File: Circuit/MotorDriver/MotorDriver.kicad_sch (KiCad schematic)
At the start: 28 parts, among them J3 Conn_01x03_Pin, J4 Conn_01x04_Pin, J5 Conn_01x06_Pin, J6 Conn_01x02_Pin, U3 DRV8316RRGFR, U4 XC6206P332MR-G

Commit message: フットプリントの割り当て完了
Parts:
- J3: footprint (none) -> OU_conn:MotorABC
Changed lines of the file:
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@@
 			)
 		)
-		(property "Footprint" ""
+		(property "Footprint" "OU_conn:MotorABC"
 			(at 132.08 140.97 0)
 			(hide yes)

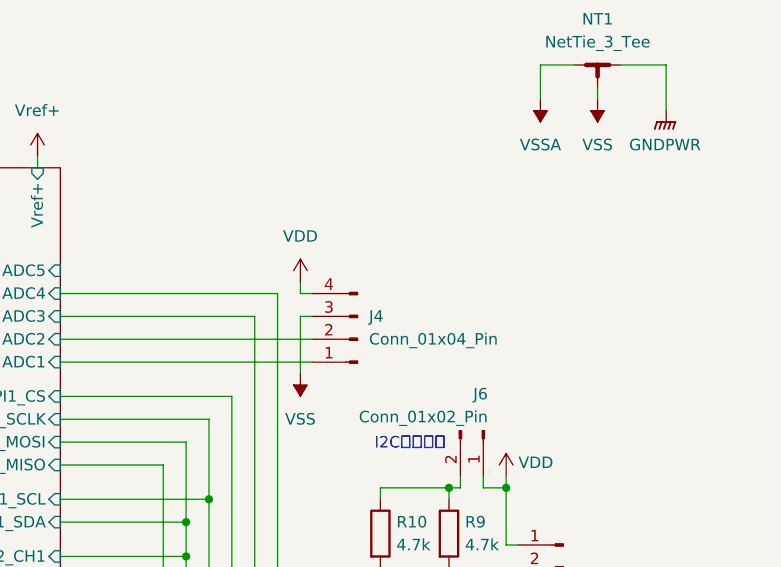
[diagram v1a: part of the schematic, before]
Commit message: フットプリントとシンボルを修正
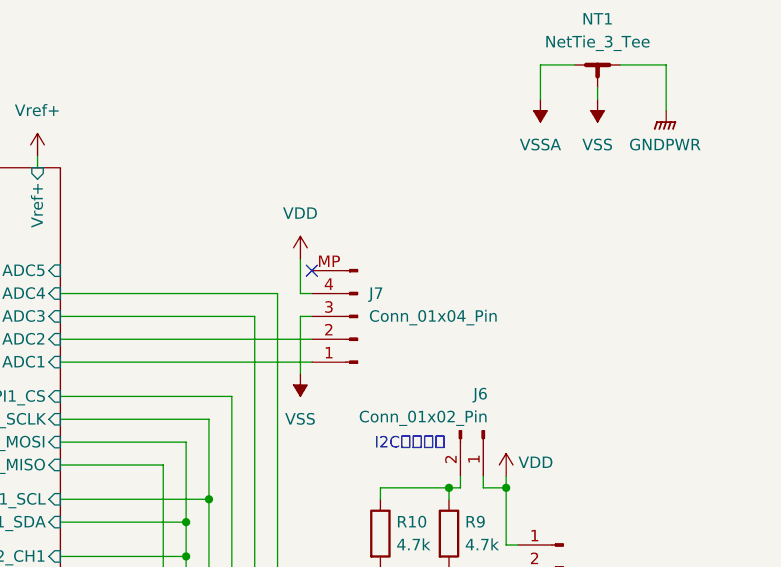
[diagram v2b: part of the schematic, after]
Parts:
- removed J4: Conn_01x04_Pin, Connector_JST:JST_GH_SM04B-GHS-TB_1x04-1MP_P1.25mm_Horizontal, symbol Connector:Conn_01x04_Pin
- added J7: Conn_01x04_Pin, Connector_JST:JST_GH_SM04B-GHS-TB_1x04-1MP_P1.25mm_Horizontal, symbol Connector:Conn_01x05_Pin
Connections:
- net STM32G4/ADC1: now also J7.1 (Pin_1)
- net STM32G4/ADC2: now also J7.2 (Pin_2)
- net VDD: now also J7.4 (Pin_4)
- net VSS: now also J7.3 (Pin_3)
- no-connect marks 3 -> 4
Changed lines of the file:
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@@
 	)
 	(no_connect
+		(at 146.05 59.69)
+	)
+	(no_connect
 		(at 123.19 172.72)
 	)
@@
 	(wire
 		(pts
-			(xy 144.78 60.96) (xy 144.78 62.23)
+			(xy 144.78 58.42) (xy 144.78 62.23)
 		)
 		(stroke
@@
 	)
 	(symbol
-		(lib_id "Connector:Conn_01x04_Pin")
-		(at 151.13 67.31 180)
-		(unit 1)
-		(body_style 1)
-		(exclude_from_sim no)
-		(in_bom yes)
-		(on_board yes)
-		(in_pos_files yes)
-		(dnp no)
-		(property "Reference" "J4"
-			(at 152.4 64.7699 0)
-			(show_name no)
-			(do_not_autoplace no)
-			(effects
-				(font
-					(size 1.27 1.27)
-				)
-				(justify right)
-			)
-		)
-		(property "Value" "Conn_01x04_Pin"
-			(at 152.4 67.3099 0)
-			(show_name no)
-			(do_not_autoplace no)
-			(effects
-				(font
-					(size 1.27 1.27)
-				)
-				(justify right)
-			)
-		)
-		(property "Footprint" "Connector_JST:JST_GH_SM04B-GHS-TB_1x04-1MP_P1.25mm_Horizontal"
-			(at 151.13 67.31 0)
-			(hide yes)
-			(show_name no)
-			(do_not_autoplace no)
-			(effects
-				(font
-					(size 1.27 1.27)
-				)
-			)
-		)
-		(property "Datasheet" ""
-			(at 151.13 67.31 0)
-			(hide yes)
-			(show_name no)
-			(do_not_autoplace no)
-			(effects
-				(font
-					(size 1.27 1.27)
-				)
-			)
-		)
-		(property "Description" "Generic connector, single row, 01x04, script generated"
-			(at 151.13 67.31 0)
-			(hide yes)
-			(show_name no)
-			(do_not_autoplace no)
-			(effects
-				(font
-					(size 1.27 1.27)
-				)
-			)
-		)
-		(pin "1"
-		)
-		(pin "2"
-		)
-		(pin "4"
-		)
-		(pin "3"
-		)
-		(instances
-			(project "MotorDriver"
-				(path "/0d88f791-841b-4934-8770-7a8a0368e67c"
-					(reference "J4")
-					(unit 1)
-				)
-			)
-		)
-	)
-	(symbol
 		(lib_id "power:VSS")
 		(at 172.6592 198.12 180)
@@
 	(symbol
 		(lib_id "power:VDD")
-		(at 144.78 60.96 0)
+		(at 144.78 58.42 0)
 		(unit 1)
 		(body_style 1)
@@
 		(fields_autoplaced yes)
 		(property "Reference" "#PWR043"
-			(at 144.78 64.77 0)
+			(at 144.78 62.23 0)
 			(hide yes)
 			(show_name no)
@@
 		)
 		(property "Value" "VDD"
-			(at 144.78 55.88 0)
+			(at 144.78 53.34 0)
 			(show_name no)
 			(do_not_autoplace no)
@@
 		)
 		(property "Footprint" ""
-			(at 144.78 60.96 0)
+			(at 144.78 58.42 0)
 			(hide yes)
 			(show_name no)
@@
 		)
 		(property "Datasheet" ""
-			(at 144.78 60.96 0)
+			(at 144.78 58.42 0)
 			(hide yes)
 			(show_name no)
@@
 		)
 		(property "Description" "Power symbol creates a global label with name \"VDD\""
-			(at 144.78 60.96 0)
+			(at 144.78 58.42 0)
 			(hide yes)
 			(show_name no)
@@
 					(unit 1)
 				)
+			)
+		)
+	)
+	(symbol
+		(lib_id "Connector:Conn_01x05_Pin")
+		(at 151.13 64.77 180)
+		(unit 1)
+		(body_style 1)
+		(exclude_from_sim no)
+		(in_bom yes)
+		(on_board yes)
+		(in_pos_files yes)
+		(dnp no)
+		(property "Reference" "J7"
+			(at 152.4 62.2299 0)
+			(show_name no)
+			(do_not_autoplace no)
+			(effects
+				(font
+					(size 1.27 1.27)
+				)
+				(justify right)
+			)
+		)
+		(property "Value" "Conn_01x04_Pin"
+			(at 152.4 64.7699 0)
+			(show_name no)
+			(do_not_autoplace no)
+			(effects
+				(font
+					(size 1.27 1.27)
+				)
+				(justify right)
+			)
+		)
+		(property "Footprint" "Connector_JST:JST_GH_SM04B-GHS-TB_1x04-1MP_P1.25mm_Horizontal"
+			(at 151.13 64.77 0)
+			(hide yes)
+			(show_name no)
+			(do_not_autoplace no)
+			(effects
+				(font
+					(size 1.27 1.27)
+				)
+			)
+		)
+		(property "Datasheet" ""
+			(at 151.13 64.77 0)
+			(hide yes)
+			(show_name no)
+			(do_not_autoplace no)
+			(effects
+				(font
+					(size 1.27 1.27)
+				)
+			)
+		)
+		(property "Description" "Generic connector, single row, 01x05, script generated"
+			(at 151.13 64.77 0)
+			(hide yes)
+			(show_name no)
+			(do_not_autoplace no)
+			(effects
+				(font
+					(size 1.27 1.27)
+				)
+			)
+		)
+		(pin "1"
+		)
+		(pin "2"
+		)
+		(pin "4"
+		)
+		(pin "3"
+		)
+		(pin "MP"
+		)
+		(instances
+			(project "MotorDriver"
+				(path "/0d88f791-841b-4934-8770-7a8a0368e67c"
+					(reference "J7")
+					(unit 1)
+				)

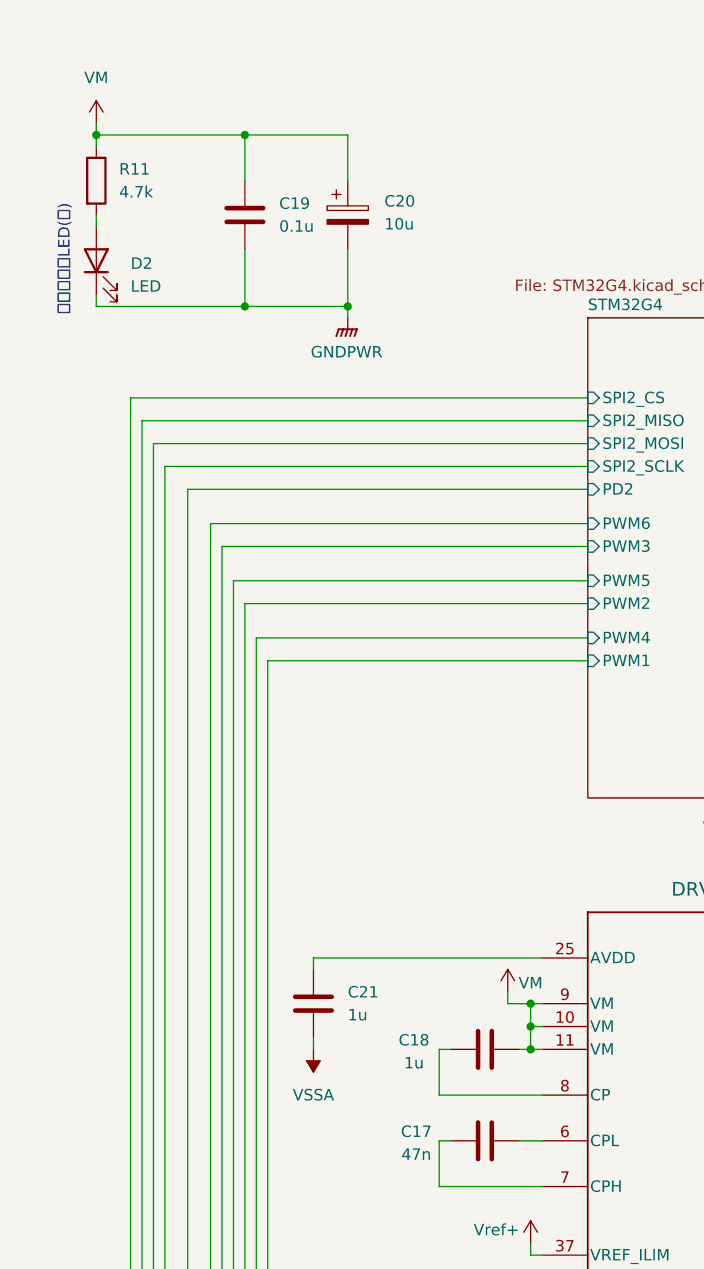
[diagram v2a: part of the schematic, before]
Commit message: 忘れていたCANトランシーバやモータ電源コネクタを追加
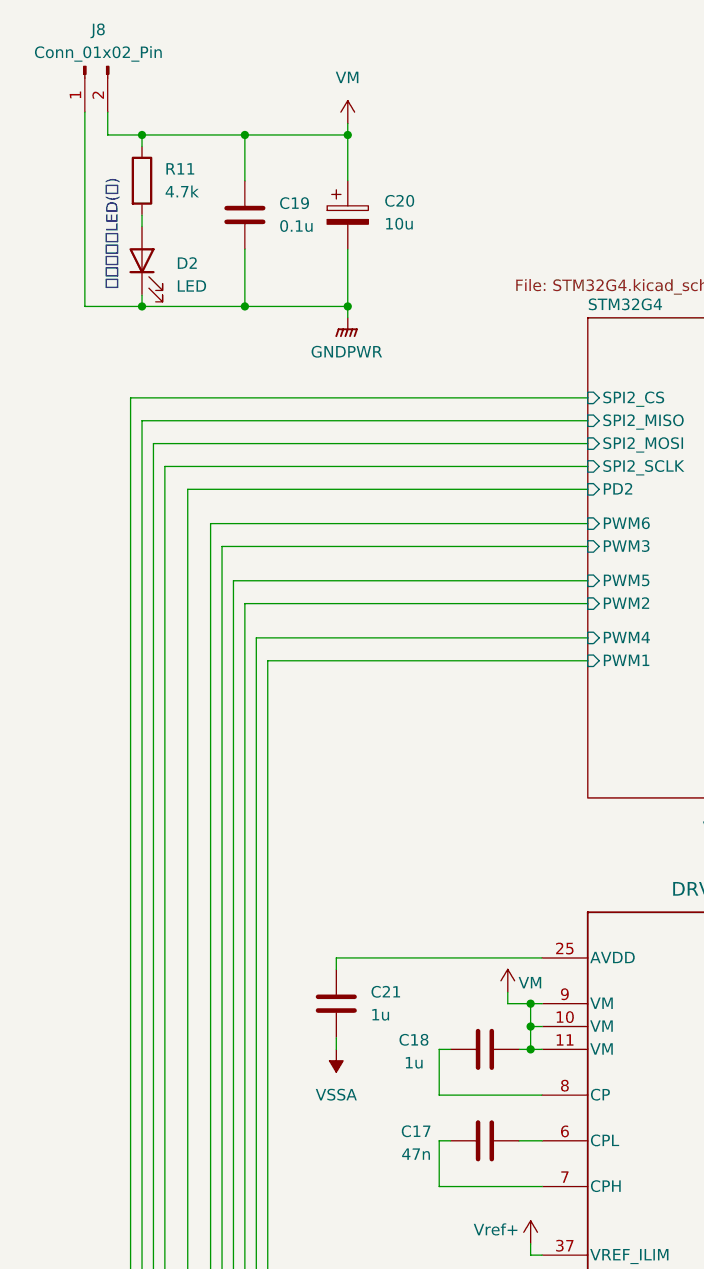
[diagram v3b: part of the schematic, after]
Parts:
- added J8: Conn_01x02_Pin, OU_conn:AMASS_XT30PW-M, symbol Connector:Conn_01x02_Pin
- NT1: footprint NetTie:NetTie-3_SMD_Pad2.0mm -> NetTie:NetTie-3_SMD_Pad0.5mm
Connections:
- net GNDPWR: now also J8.1 (Pin_1)
- net VM: now also J8.2 (Pin_2)
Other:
- moved on the sheet: C21, D2, R11
